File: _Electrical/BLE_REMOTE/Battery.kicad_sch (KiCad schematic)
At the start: 29 parts, among them J4 Battery, Q1 IRLML6244, Q1 RE1C002UNTCL, Q2 IRLML6244, SW1 SW_Push, U3 IRF7319TRPBF, U3 MCP65R41

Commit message: started PCB design
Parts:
- removed C13: 0.1uF, Capacitor_SMD:C_0402_1005Metric_Pad0.74x0.62mm_HandSolder, symbol Device:C
- removed C13: 10uF, Capacitor_SMD:C_0402_1005Metric_Pad0.74x0.62mm_HandSolder, symbol Device:C
- removed Q1, Q2 (x2): IRLML6244, Package_TO_SOT_SMD:SOT-23, symbol Transistor_FET:IRLML6244
- removed Q1: RE1C002UNTCL, _Parts:DIO_RB558WMF_ROM, symbol Simulation_SPICE:NMOS
- removed R14: 330, Resistor_SMD:R_0402_1005Metric_Pad0.72x0.64mm_HandSolder, symbol Device:R
- removed R16 (x2), R4: 47k, Resistor_SMD:R_0402_1005Metric_Pad0.72x0.64mm_HandSolder, symbol Device:R
- removed R25: 2.2K, Resistor_SMD:R_0402_1005Metric_Pad0.72x0.64mm_HandSolder, symbol Device:R
- removed SW1: SW_Push, symbol Switch:SW_Push
- added Q3: PMOS, Package_TO_SOT_SMD:SOT-323_SC-70_Handsoldering, symbol Simulation_SPICE:PMOS
- R17: value 16k -> 173k
- R18: value 9k1 -> 100k
- SW1: footprint (none) -> Button_Switch_SMD:SW_Push_1P1T_NO_6x6mm_H9.5mm
- renumbered U3 to U5
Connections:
- net BAT_IN is gone; now on net VBAT: U3.6 (V+)
- net BAT+: no longer D3.1 (K), R17.1
- net GND: now also Q3.1 (D)
- net VBAT: now also R17.1
- net at C13.2, R10.1, SW1.1: now also D3.1 (K)
- net BAT_CTRL: now reaches D3.2 (A), R25.1, R25.2
- net BAT_CTRL: now also Q3.3 (S)
- net LOW_BAT: no longer names the net of R15.2, U3.1
- net LOW_BAT: now also Q3.2 (G)
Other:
- moved on the sheet: C13, C15, C17, D3, J4, R10, R15, R16, R17, R18, R25, SW1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

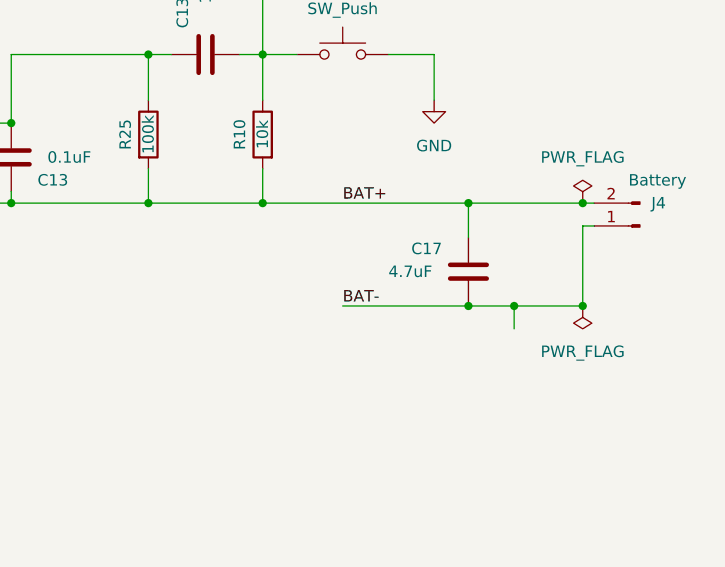
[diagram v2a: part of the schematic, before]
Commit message: Finished initial PCB draft
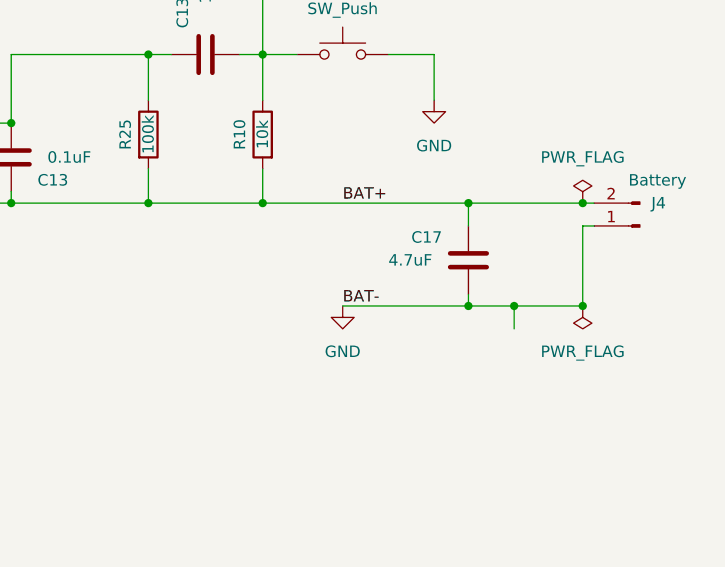
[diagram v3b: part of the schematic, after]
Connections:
- net BAT- is gone; now on net GND: C17.2, J4.1 (Pin_1)
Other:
- moved on the sheet: C17

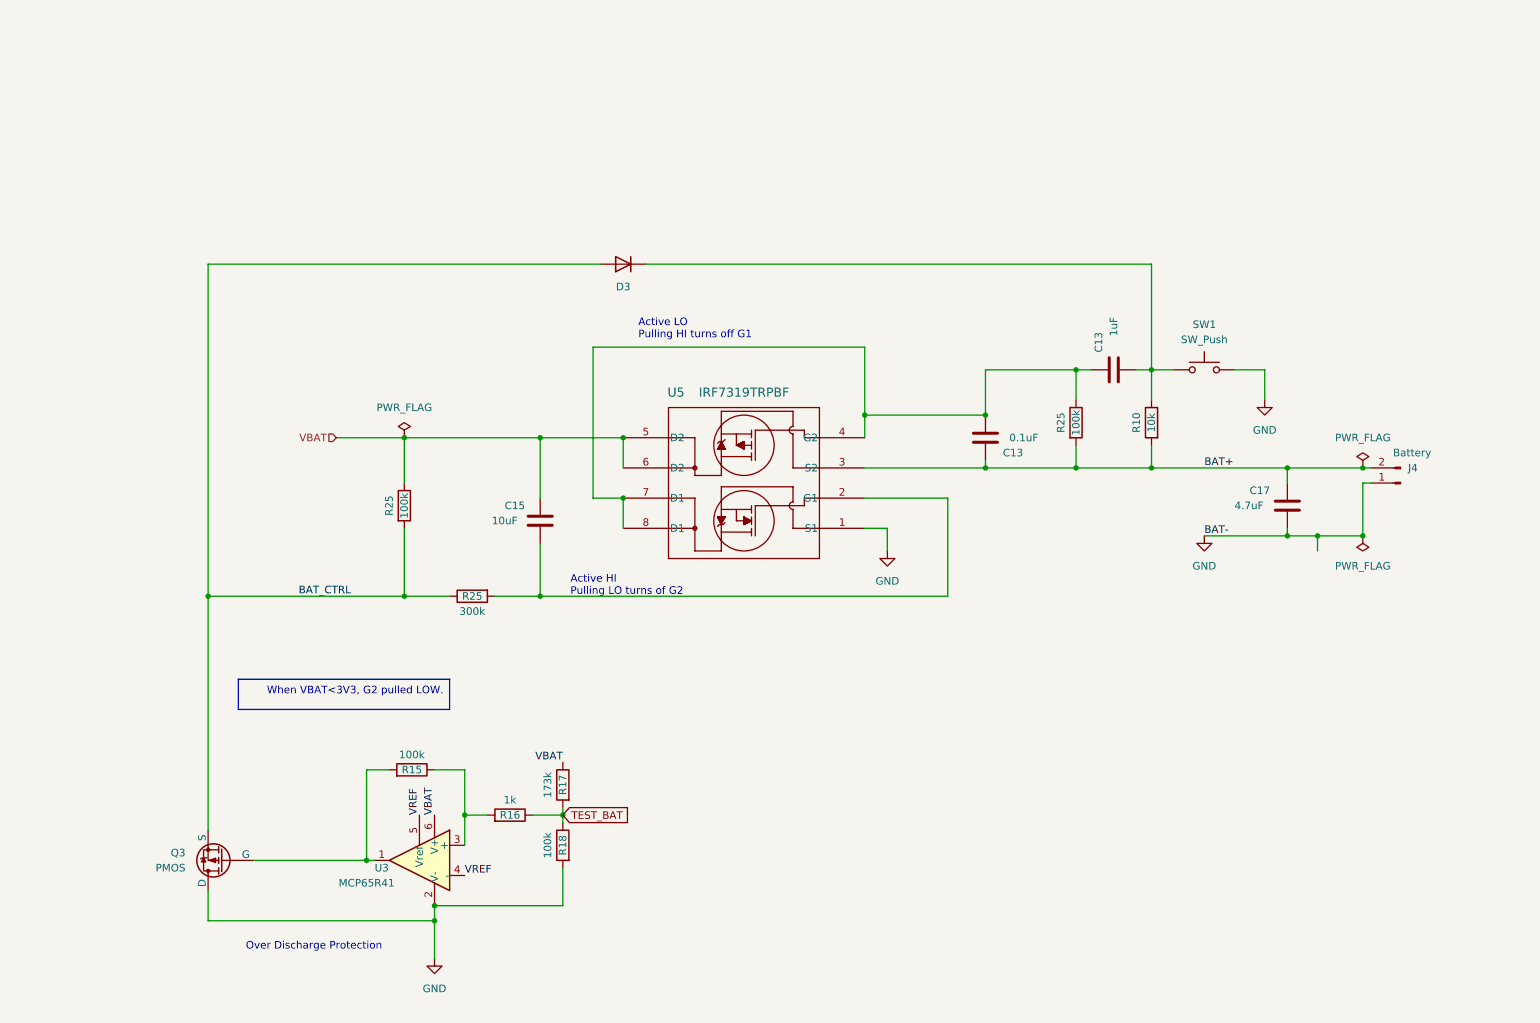
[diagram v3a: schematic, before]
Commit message: JLCPCB parts selected
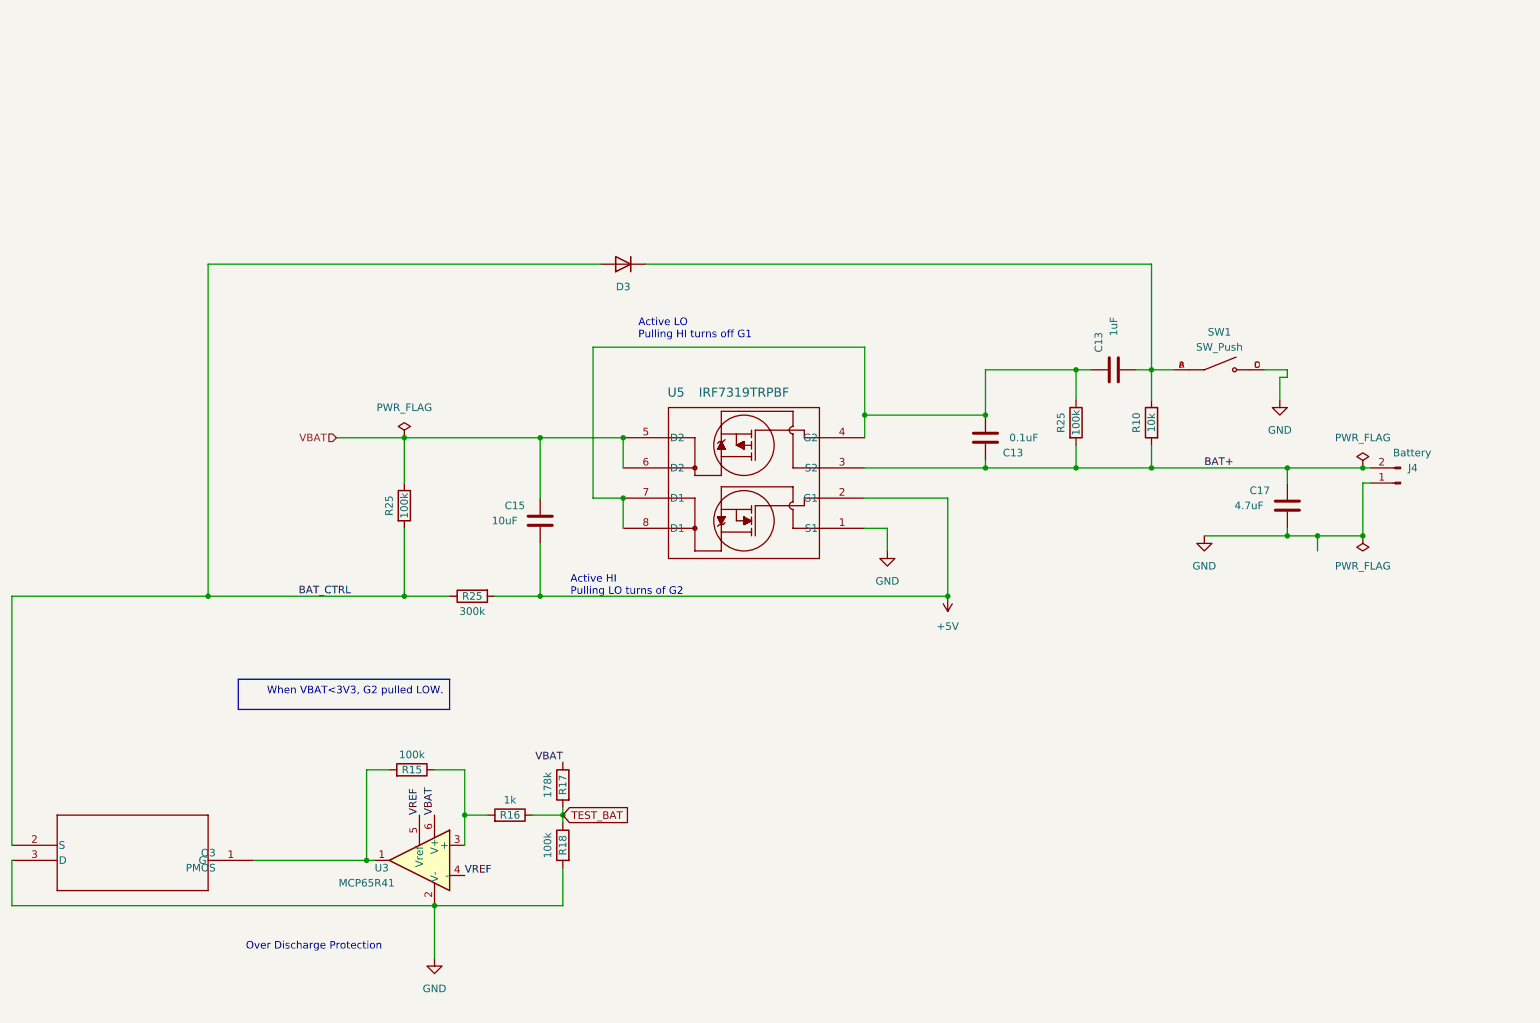
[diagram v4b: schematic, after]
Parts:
- Q3: footprint Package_TO_SOT_SMD:SOT-323_SC-70_Handsoldering -> _Parts:SOT-23-3L_AOS; symbol Simulation_SPICE:PMOS -> AO3401A:AO3401A; JLCPCB Part# (none) -> C15127; LCSC Part # (none) -> C15127; Part DMP2160UW-7 -> AO3401A
- R17: value 173k -> 178k; LCSC Part # (none) -> C102842
- SW1: footprint Button_Switch_SMD:SW_Push_1P1T_NO_6x6mm_H9.5mm -> _Parts:SW_TS-1187A-B-A-B; symbol Switch:SW_Push -> TS-1187A-B-A-B:TS-1187A-B-A-B; Availability (none) -> Not in stock; Check_prices (none) -> https://www.snapeda.com/parts/TS-1187A-B-A-B/XKB+Industrial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; JLCPCB Part# (none) -> C318884; LCSC Part # (none) -> C102842; MANUFACTURER (none) -> XKB Industrial Precision; MAXIMUM_PACKAGE_HEIGHT (none) -> 1.5mm; MF (none) -> XKB Industrial Precision; MP (none) -> TS-1187A-B-A-B; PARTREV (none) -> A0; Package (none) -> Package; Price (none) -> None; STANDARD (none) -> Manufacturer Recommendations; SnapEDA_Link (none) -> https://www.snapeda.com/parts/TS-1187A-B-A-B/XKB+Industrial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
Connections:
- net BAT_CTRL: now also Q3.2 (S); no longer Q3.3 (S)
- net GND: now also Q3.3 (D), SW1.C, SW1.D; no longer Q3.1 (D), SW1.2
- net at C13.2, D3.1 (K), R10.1: now also SW1.A, SW1.B; no longer SW1.1
- net at R15.2, U3.1: now also Q3.1 (G); no longer Q3.2 (G)
- net +5V: now reaches C15.2, R25.2, U5.2 (G1)

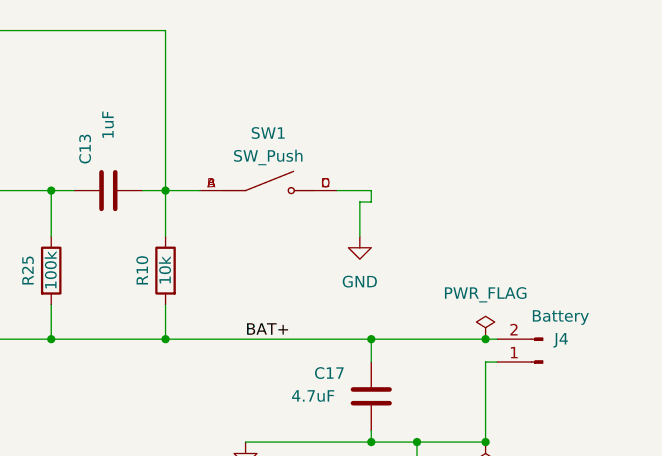
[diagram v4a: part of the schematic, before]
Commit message: Adjusted components and changed buttons
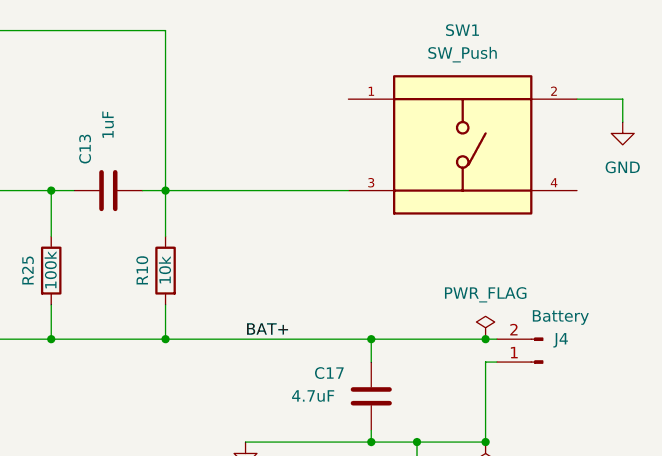
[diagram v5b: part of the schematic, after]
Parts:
- SW1: footprint _Parts:SW_TS-1187A-B-A-B -> _Parts:SW_TS02-66-120-BK-260-LCR-D; symbol TS-1187A-B-A-B:TS-1187A-B-A-B -> TS02-66-120-BK-260-LCR-D:TS02-66-120-BK-260-LCR-D; JLCPCB Part# C318884 -> (none); LCSC Part # C102842 -> (none); MANUFACTURER XKB Industrial Precision -> CUI Devices; PARTREV A0 -> 1.0; Part (none) -> TS02-66-120-BK-260-LCR-D
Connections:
- net GND: now also SW1.2; no longer SW1.C, SW1.D
- net at C13.2, D3.1 (K), R10.1: now also SW1.3; no longer SW1.A, SW1.B

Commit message: asdasat
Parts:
- added C17: 2.2uF, Capacitor_SMD:C_0603_1608Metric_Pad1.08x0.95mm_HandSolder, symbol Device:C
- C13: value 0.1uF -> 100nF; LCSC Part # (none) -> C1525
- C13: LCSC Part # (none) -> C52923
- C15: LCSC Part # (none) -> C15525
- C17: LCSC Part # (none) -> C1779
- D3: LCSC Part # (none) -> C2128
- J4: now left out of the parts list
- R10: LCSC Part # (none) -> C25744
- R15, R25: LCSC Part # (none) -> C25741
- R16: LCSC Part # (none) -> C11702
- R17: value 178k -> 150k; footprint Resistor_SMD:R_0402_1005Metric_Pad0.72x0.64mm_HandSolder -> Resistor_SMD:R_0603_1608Metric_Pad0.98x0.95mm_HandSolder; LCSC Part # C102842 -> C22807; Part RC0402FR-0716KL -> (none)
- R18: LCSC Part # (none) -> C25741; Part RC0402FR-079K1L -> RC0402FR-07100KL
- R25: footprint Resistor_SMD:R_0402_1005Metric_Pad0.72x0.64mm_HandSolder -> Resistor_SMD:R_0603_1608Metric_Pad0.98x0.95mm_HandSolder; LCSC Part # (none) -> C23024
- U3: LCSC Part # (none) -> C219181
- U5: LCSC Part # (none) -> C5123893
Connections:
- net BAT+: now also C17.1
- net GND: now also SW1.1, C17.2
- net at C13.2, D3.1 (K), R10.1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: now also SW1.4
